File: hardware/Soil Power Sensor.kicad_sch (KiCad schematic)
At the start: 0 parts

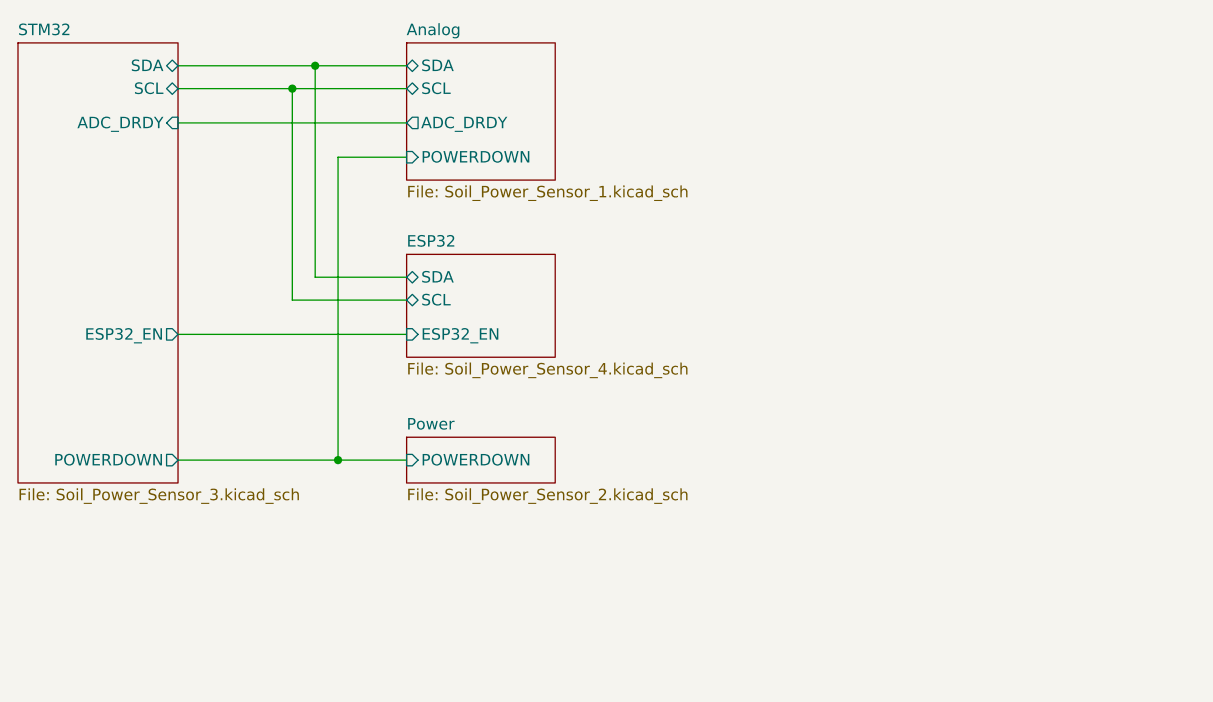
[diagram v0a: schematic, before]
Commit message: Adding general improvements to sensor PCB
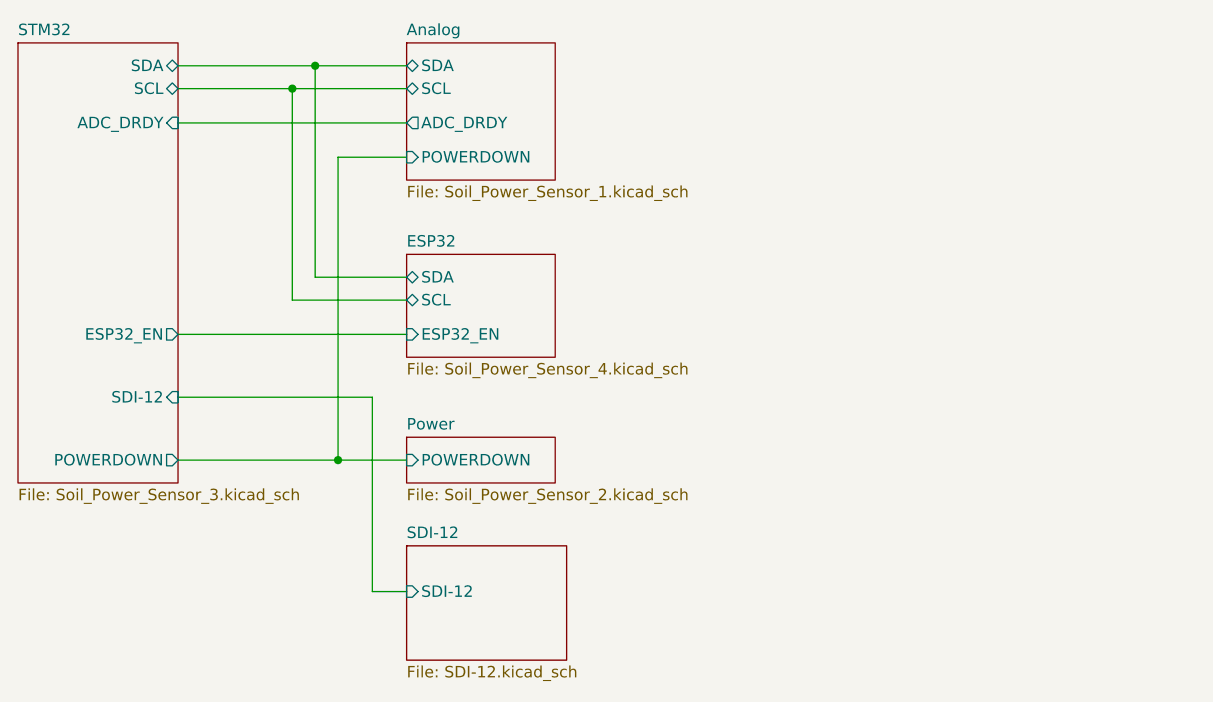
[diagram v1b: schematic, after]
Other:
- added sheet SDI-12 (SDI-12.kicad_sch)
- sheet STM32 ports: added SDI-12; removed none
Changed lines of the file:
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@@
+    (stroke (width 0) (type default))
+  )
+  (wire (pts (xy 158.75 111.76) (xy 137.16 111.76))
+    (stroke (width 0) (type default))
+  )
+  (wire (pts (xy 158.75 133.35) (xy 158.75 111.76))
     (stroke (width 0) (type default))
   )
   (wire (pts (xy 149.86 77.47) (xy 162.56 77.47))
+    (stroke (width 0) (type default))
+  )
+  (wire (pts (xy 162.56 133.35) (xy 158.75 133.35))
     (stroke (width 0) (type default))
   )
@@
       (effects (font (size 1.27 1.27)) (justify right))
     )
+    (pin "SDI-12" input (at 137.16 111.76 0)
+      (effects (font (size 1.27 1.27)) (justify right))
+    )
     (instances
       (project "Soil Power Sensor"
@@
       )
     )
+  )
+  (sheet (at 162.56 128.27) (size 17.78 12.7) (fields_autoplaced)
+    (stroke (width 0.1524) (type solid))
+    (fill (color 0 0 0 0.0000))
+    (property "Sheetname" "SDI-12" (at 162.56 127.5584 0)
+      (effects (font (size 1.27 1.27)) (justify left bottom))
+    )
+    (property "Sheetfile" "SDI-12.kicad_sch" (at 162.56 141.5546 0)
+      (effects (font (size 1.27 1.27)) (justify left top))
+    )
+    (pin "SDI-12" input (at 162.56 133.35 180)
+      (effects (font (size 1.27 1.27)) (justify left))
+    )
+    (instances
+      (project "Soil Power Sensor"
+        (path "/5300ec4d-4648-40a1-8d89-4fa6b3bf32a3" (page "6"))
+      )
+    )

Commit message: Moved hardware components to new sheet
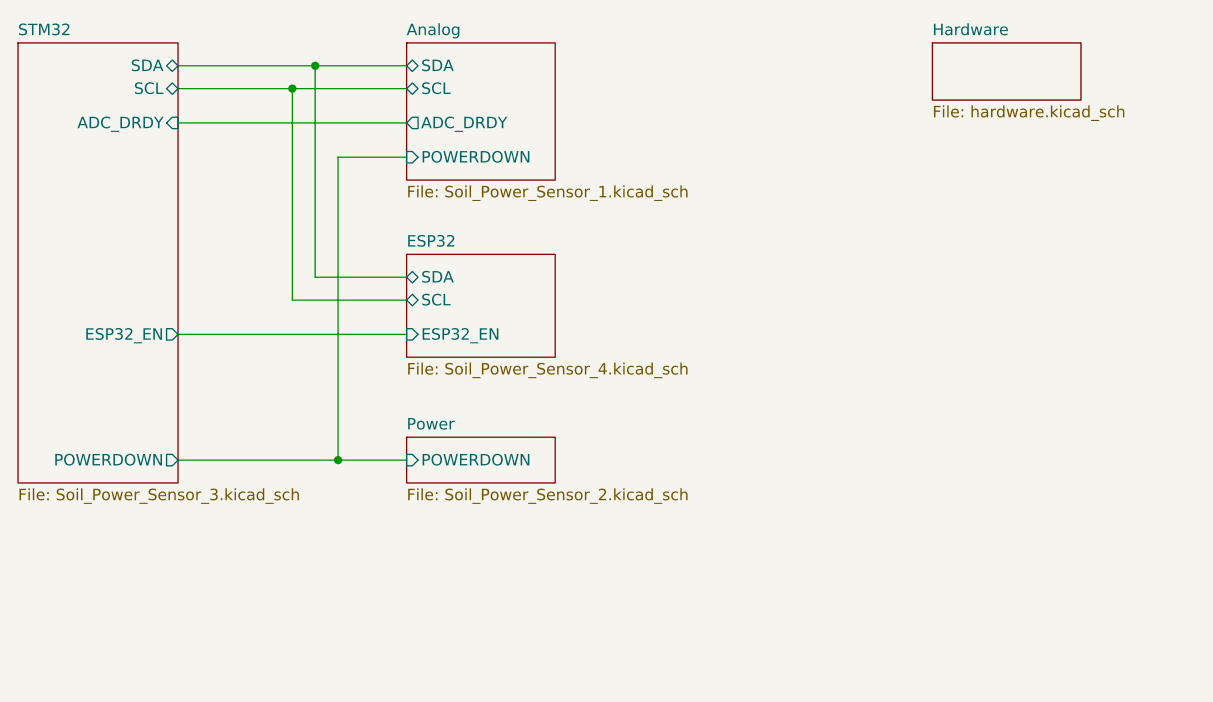
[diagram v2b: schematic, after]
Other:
- removed sheet SDI-12
- added sheet Hardware (hardware.kicad_sch)
- sheet STM32 ports: added none; removed SDI-12
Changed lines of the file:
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@@
-    (stroke (width 0) (type default))
-  )
-  (wire (pts (xy 158.75 111.76) (xy 137.16 111.76))
-    (stroke (width 0) (type default))
-  )
-  (wire (pts (xy 158.75 133.35) (xy 158.75 111.76))
     (stroke (width 0) (type default))
   )
   (wire (pts (xy 149.86 77.47) (xy 162.56 77.47))
-    (stroke (width 0) (type default))
-  )
-  (wire (pts (xy 162.56 133.35) (xy 158.75 133.35))
     (stroke (width 0) (type default))
   )
@@
       (effects (font (size 1.27 1.27)) (justify right))
     )
-    (pin "SDI-12" input (at 137.16 111.76 0)
-      (effects (font (size 1.27 1.27)) (justify right))
-    )
     (instances
       (project "Soil Power Sensor"
         (path "/5300ec4d-4648-40a1-8d89-4fa6b3bf32a3" (page "3"))
-      )
-    )
-  )
-  (sheet (at 162.56 128.27) (size 17.78 12.7) (fields_autoplaced)
-    (stroke (width 0.1524) (type solid))
-    (fill (color 0 0 0 0.0000))
-    (property "Sheetname" "SDI-12" (at 162.56 127.5584 0)
-      (effects (font (size 1.27 1.27)) (justify left bottom))
-    )
-    (property "Sheetfile" "SDI-12.kicad_sch" (at 162.56 141.5546 0)
-      (effects (font (size 1.27 1.27)) (justify left top))
-    )
-    (pin "SDI-12" input (at 162.56 133.35 180)
-      (effects (font (size 1.27 1.27)) (justify left))
-    )
-    (instances
-      (project "Soil Power Sensor"
-        (path "/5300ec4d-4648-40a1-8d89-4fa6b3bf32a3" (page "6"))
       )
     )
@@
       )
     )
+  )
+  (sheet (at 220.98 72.39) (size 16.51 6.35) (fields_autoplaced)
+    (stroke (width 0.1524) (type solid))
+    (fill (color 0 0 0 0.0000))
+    (property "Sheetname" "Hardware" (at 220.98 71.6784 0)
+      (effects (font (size 1.27 1.27)) (justify left bottom))
+    )
+    (property "Sheetfile" "hardware.kicad_sch" (at 220.98 79.3246 0)
+      (effects (font (size 1.27 1.27)) (justify left top))
+    )
+    (instances
+      (project "Soil Power Sensor"
+        (path "/5300ec4d-4648-40a1-8d89-4fa6b3bf32a3" (page "5"))
+      )
+    )

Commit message: Fixed ERC errors
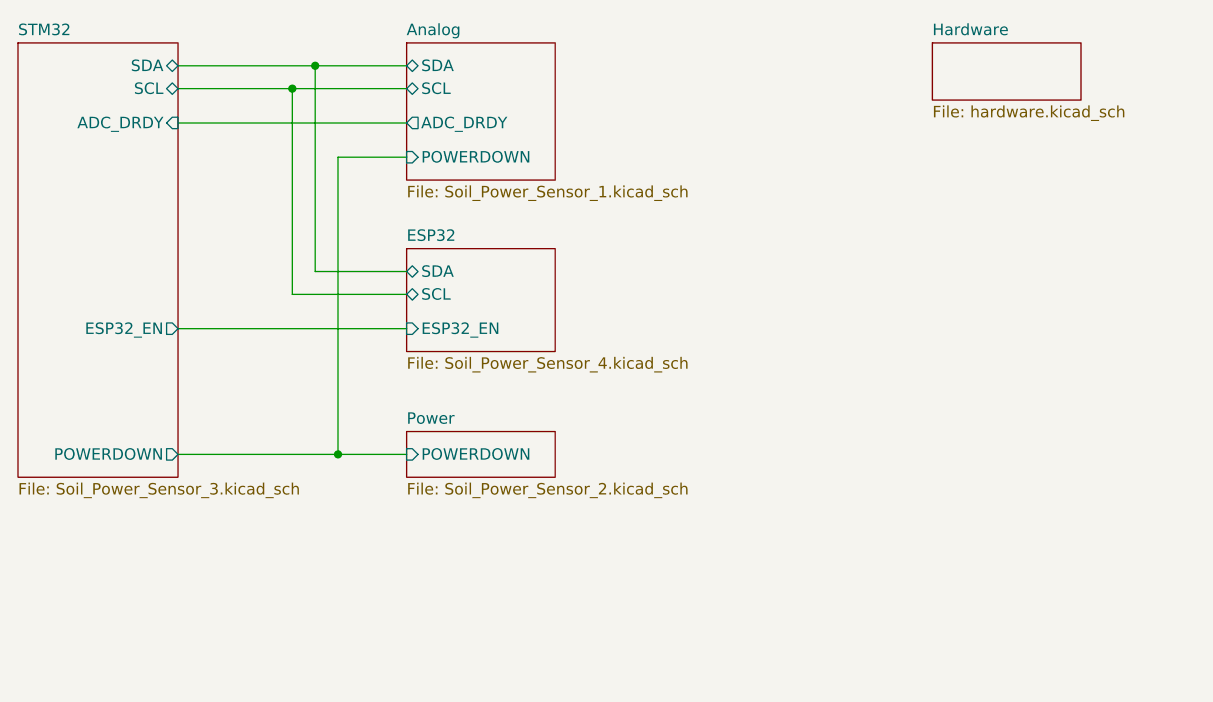
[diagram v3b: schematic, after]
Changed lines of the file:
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@@
     (company "jlab")
   )
-  (junction (at 154.94 118.745) (diameter 0) (color 0 0 0 0)
+  (junction (at 152.4 74.93) (diameter 0) (color 0 0 0 0)
   )
-  (junction (at 152.4 74.93) (diameter 0) (color 0 0 0 0)
+  (junction (at 154.94 118.11) (diameter 0) (color 0 0 0 0)
   )
   (junction (at 149.86 77.47) (diameter 0) (color 0 0 0 0)
@@
     (stroke (width 0) (type default))
   )
+  (wire (pts (xy 162.56 104.14) (xy 137.16 104.14))
+    (stroke (width 0) (type default))
+  )
   (wire (pts (xy 149.86 77.47) (xy 162.56 77.47))
     (stroke (width 0) (type default))
   )
-  (wire (pts (xy 162.56 100.965) (xy 149.86 100.965))
+  (wire (pts (xy 162.56 100.33) (xy 149.86 100.33))
     (stroke (width 0) (type default))
   )
@@
     (stroke (width 0) (type default))
   )
-  (wire (pts (xy 154.94 85.09) (xy 154.94 118.745))
-    (stroke (width 0) (type default))
-  )
-  (wire (pts (xy 137.16 104.775) (xy 162.56 104.775))
+  (wire (pts (xy 154.94 85.09) (xy 154.94 118.11))
     (stroke (width 0) (type default))
   )
@@
     (stroke (width 0) (type default))
   )
-  (wire (pts (xy 154.94 118.745) (xy 162.56 118.745))
+  (wire (pts (xy 154.94 118.11) (xy 162.56 118.11))
     (stroke (width 0) (type default))
   )
-  (wire (pts (xy 149.86 77.47) (xy 149.86 100.965))
+  (wire (pts (xy 149.86 77.47) (xy 149.86 100.33))
     (stroke (width 0) (type default))
   )
-  (wire (pts (xy 162.56 98.425) (xy 152.4 98.425))
+  (wire (pts (xy 162.56 97.79) (xy 152.4 97.79))
     (stroke (width 0) (type default))
   )
-  (wire (pts (xy 152.4 74.93) (xy 152.4 98.425))
+  (wire (pts (xy 152.4 74.93) (xy 152.4 97.79))
     (stroke (width 0) (type default))
   )
-  (wire (pts (xy 137.16 118.745) (xy 154.94 118.745))
+  (wire (pts (xy 137.16 118.11) (xy 154.94 118.11))
     (stroke (width 0) (type default))
   )
-  (sheet (at 162.56 95.885) (size 16.51 11.43) (fields_autoplaced)
+  (sheet (at 162.56 95.25) (size 16.51 11.43) (fields_autoplaced)
     (stroke (width 0) (type solid))
     (fill (color 0 0 0 0.0000))
-    (property "Sheetname" "ESP32" (at 162.56 95.1734 0)
+    (property "Sheetname" "ESP32" (at 162.56 94.5384 0)
       (effects (font (size 1.27 1.27)) (justify left bottom))
     )
-    (property "Sheetfile" "Soil_Power_Sensor_4.kicad_sch" (at 162.56 107.8996 0)
+    (property "Sheetfile" "Soil_Power_Sensor_4.kicad_sch" (at 162.56 107.2646 0)
       (effects (font (size 1.27 1.27)) (justify left top))
     )
-    (pin "ESP32_EN" input (at 162.56 104.775 180)
+    (pin "ESP32_EN" input (at 162.56 104.14 180)
       (effects (font (size 1.27 1.27)) (justify left))
     )
-    (pin "SCL" bidirectional (at 162.56 100.965 180)
+    (pin "SCL" bidirectional (at 162.56 100.33 180)
       (effects (font (size 1.27 1.27)) (justify left))
     )
-    (pin "SDA" bidirectional (at 162.56 98.425 180)
+    (pin "SDA" bidirectional (at 162.56 97.79 180)
       (effects (font (size 1.27 1.27)) (justify left))
     )
@@
     )
   )
-  (sheet (at 119.38 72.39) (size 17.78 48.895) (fields_autoplaced)
+  (sheet (at 119.38 72.39) (size 17.78 48.26) (fields_autoplaced)
     (stroke (width 0) (type solid))
     (fill (color 0 0 0 0.0000))
@@
       (effects (font (size 1.27 1.27)) (justify left bottom))
     )
-    (property "Sheetfile" "Soil_Power_Sensor_3.kicad_sch" (at 119.38 121.8696 0)
+    (property "Sheetfile" "Soil_Power_Sensor_3.kicad_sch" (at 119.38 121.2346 0)
       (effects (font (size 1.27 1.27)) (justify left top))
     )
-    (pin "ESP32_EN" output (at 137.16 104.775 0)
+    (pin "ESP32_EN" output (at 137.16 104.14 0)
       (effects (font (size 1.27 1.27)) (justify right))
     )
@@
       (effects (font (size 1.27 1.27)) (justify right))
     )
-    (pin "POWERDOWN" output (at 137.16 118.745 0)
+    (pin "POWERDOWN" output (at 137.16 118.11 0)
       (effects (font (size 1.27 1.27)) (justify right))
     )
@@
     )
   )
-  (sheet (at 162.56 116.205) (size 16.51 5.08) (fields_autoplaced)
+  (sheet (at 162.56 115.57) (size 16.51 5.08) (fields_autoplaced)
     (stroke (width 0) (type solid))
     (fill (color 0 0 0 0.0000))
-    (property "Sheetname" "Power" (at 162.56 115.4934 0)
+    (property "Sheetname" "Power" (at 162.56 114.8584 0)
       (effects (font (size 1.27 1.27)) (justify left bottom))
     )
-    (property "Sheetfile" "Soil_Power_Sensor_2.kicad_sch" (at 162.56 121.8696 0)
+    (property "Sheetfile" "Soil_Power_Sensor_2.kicad_sch" (at 162.56 121.2346 0)
       (effects (font (size 1.27 1.27)) (justify left top))
     )
-    (pin "POWERDOWN" input (at 162.56 118.745 180)
+    (pin "POWERDOWN" input (at 162.56 118.11 180)
       (effects (font (size 1.27 1.27)) (justify left))
     )
